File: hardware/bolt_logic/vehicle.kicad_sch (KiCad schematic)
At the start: 43 parts, among them CN1 GM X1 48-way, J3 AUX I/O, U20 BTS133TC, U21 BTS133TC, U22 BTS133TC, U23 SN65HVD234

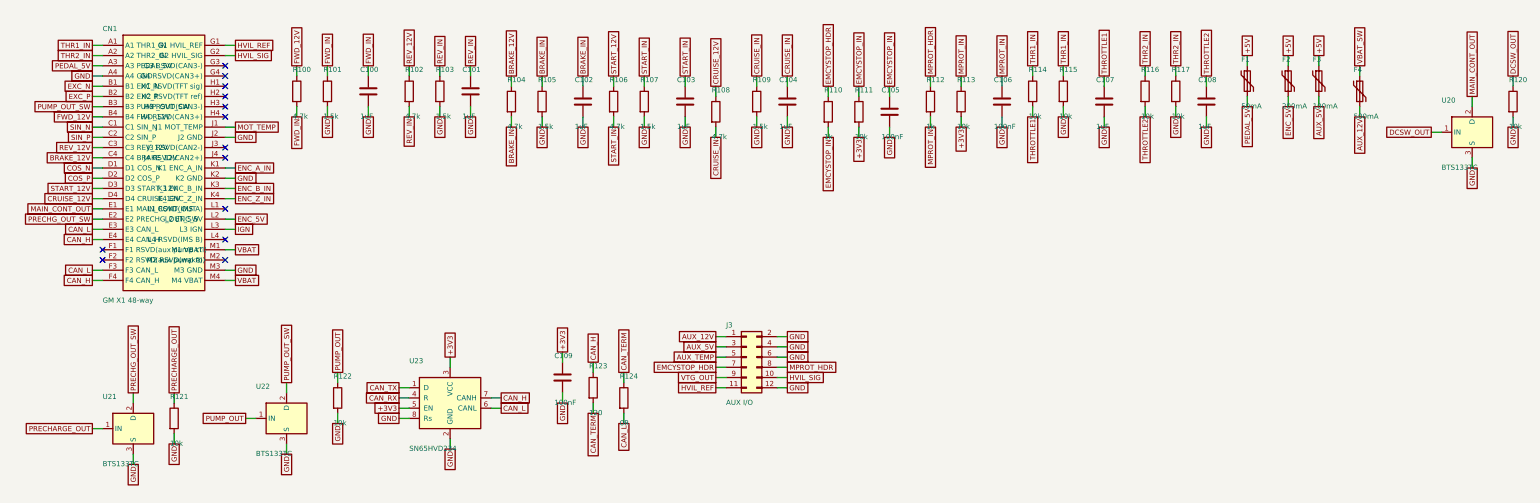
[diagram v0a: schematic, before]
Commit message: Remove the aux header (J3) and V6 leftovers: only CN1, CN2 and programming
Owner: the only connections on the board are CN1, CN2 and what is needed
to program it (J1 SWD, J4 ESP32).

- Removed J3 and what only served it: aux 12 V / 5 V outputs (F3, F4),
  aux temperature pull-up and filter (R56, C67; mux 1Y1 grounded), the
  emergency-stop / motor-protection header resistors and caps (R110,
  R112, C105, C106; the 10k pull-ups stay, so the firmware reads OK).
- CN1 G1/G2 (HVIL) only went to J3: now reserved positions.
- PC11 (VTG_OUT) and PC5 (SPEED_OUT, never connected) now NC.
- Re-placed and re-routed: 241 parts, DRC 0 violations, 0 unconnected.
- Docs: 03 (pin map, 4.10, 4.12, 4.13, CN1 table), 04, 05 updated;
  SWD header described as the 5-pin part it is.

Co-Authored-By: Claude Opus 5.5 <noreply@anthropic.com>
Claude-Session: https://claude.ai/code/session_01KW1M8KfVLc83FDDiK2YEWM
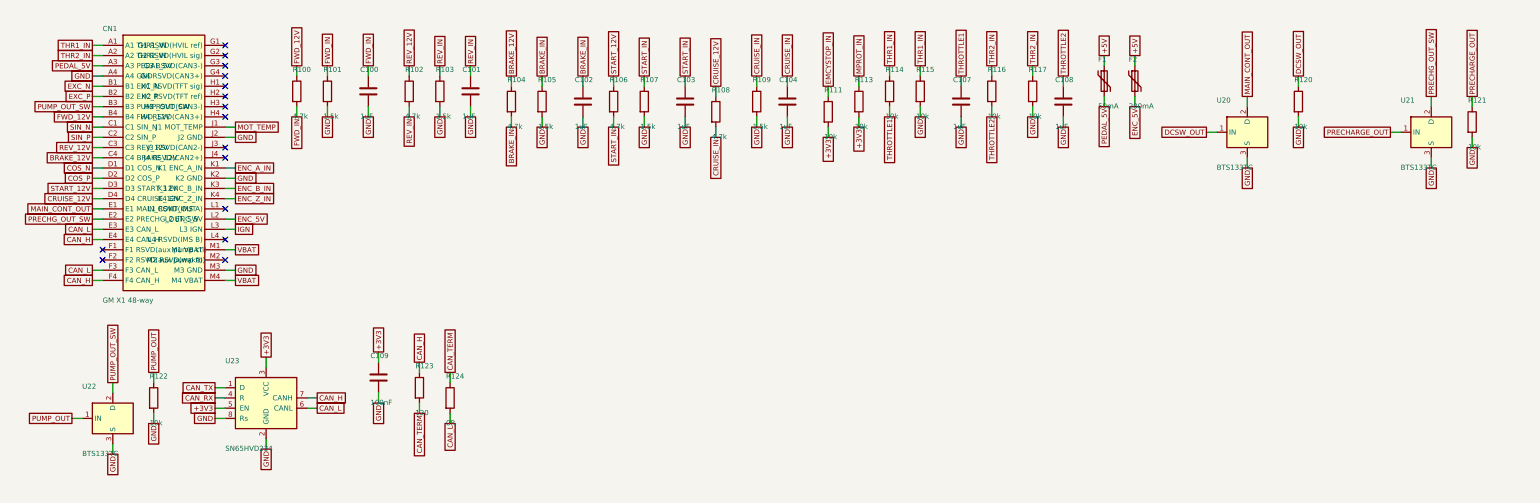
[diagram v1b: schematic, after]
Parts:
- removed C105, C106: 100nF, Capacitor_SMD:C_0805_2012Metric, symbol Device:C
- removed F3: 100mA, Fuse:Fuse_1206_3216Metric, symbol Device:Polyfuse
- removed F4: 500mA, Fuse:Fuse_1812_4532Metric, symbol Device:Polyfuse
- removed J3: AUX I/O, Connector_PinHeader_2.54mm:PinHeader_2x06_P2.54mm_Vertical, symbol Connector_Generic:Conn_02x06_Odd_Even
- removed R110, R112: 1k, Resistor_SMD:R_0805_2012Metric, symbol Device:R
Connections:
- net HVIL_REF: no longer names the net of CN1.G1 (G1 RSVD(HVIL ref))
- net HVIL_SIG: no longer names the net of CN1.G2 (G2 RSVD(HVIL sig))
- no-connect marks 13 -> 15
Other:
- moved on the sheet: C107, C108, C109, F1, F2, R111, R113, R114, R115, R116, R117, R120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
